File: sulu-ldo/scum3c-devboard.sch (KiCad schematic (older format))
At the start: 36 parts, among them J1 Conn_02x11_Odd_Even, J2 Conn_02x10_Odd_Even, J3 Conn_02x05_Odd_Even, J4 Conn_01x01_Male, U2 S-85S1AB18-I6T1U, U3 S-85S1AB11-I6T1U, U9AB1 ICM-20948

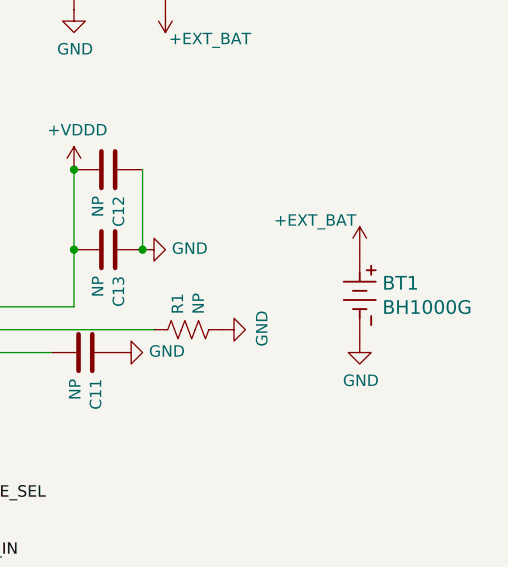
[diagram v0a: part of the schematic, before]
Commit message: updated ldo with 3d model from reg
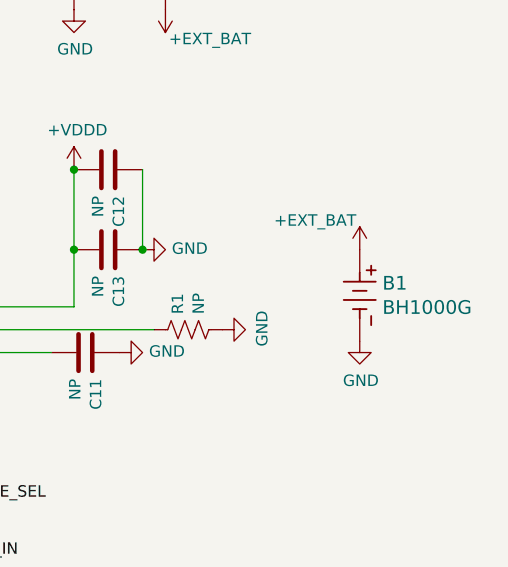
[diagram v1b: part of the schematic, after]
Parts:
- removed BT1: BH1000G, downloaded_libs:BH1000G, symbol BH1000G:BH1000G
- added B1: BH1000G, downloaded_libs:BH1000G, symbol BH1000G:BH1000G
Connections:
- net +EXT_BAT: now also B1.2
- net GND: now also B1.1
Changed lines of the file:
@@
-$EndComp
-$Comp
-L BH1000G:BH1000G BT1
-U 1 1 61316963
-P 10000 2400
-F 0 "BT1" V 10147 2499 60  0000 L CNN
-F 1 "BH1000G" V 10253 2499 60  0000 L CNN
-F 2 "downloaded_libs:BH1000G" H 10150 2040 60  0001 C CNN
-F 3 "" H 10000 2400 60  0000 C CNN
-	1    10000 2400
-	0    1    1    0
 $EndComp
 $Comp
@@
 Text Label 1200 5300 2    50   ~ 0
 1.1V_IN
+$Comp
+L BH1000G:BH1000G B1
+U 1 1 6131F561
+P 10000 2400
+F 0 "B1" V 10147 2499 60  0000 L CNN
+F 1 "BH1000G" V 10253 2499 60  0000 L CNN
+F 2 "downloaded_libs:BH1000G" H 10150 2040 60  0001 C CNN
+F 3 "" H 10000 2400 60  0000 C CNN
+	1    10000 2400
+	0    1    1    0
+$EndComp
 $EndSCHEMATC

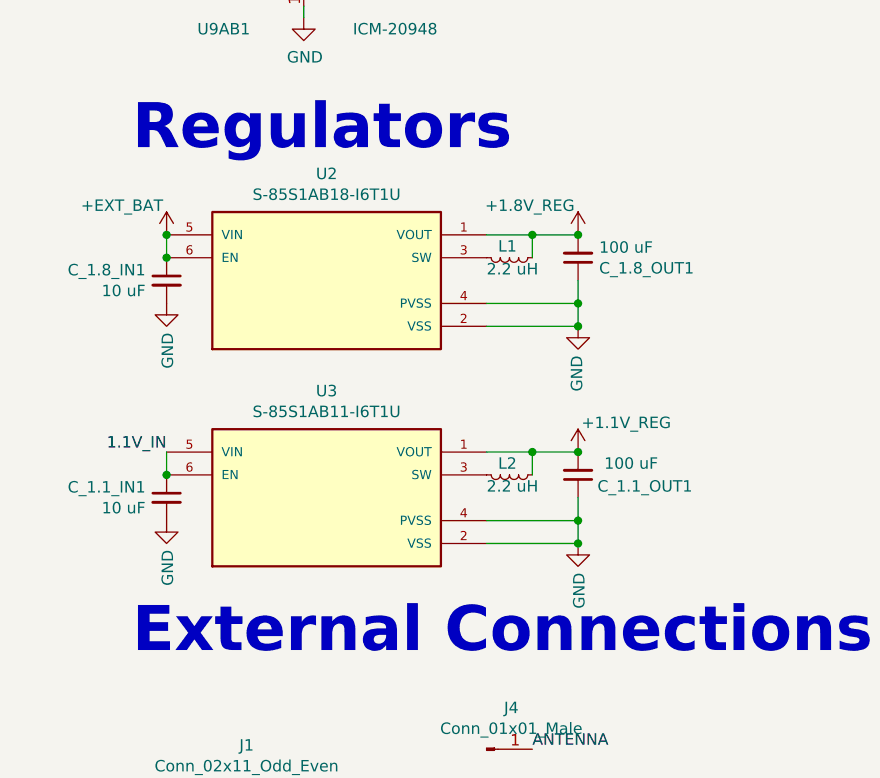
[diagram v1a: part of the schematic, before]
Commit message: checked out ldo version from ldo branch
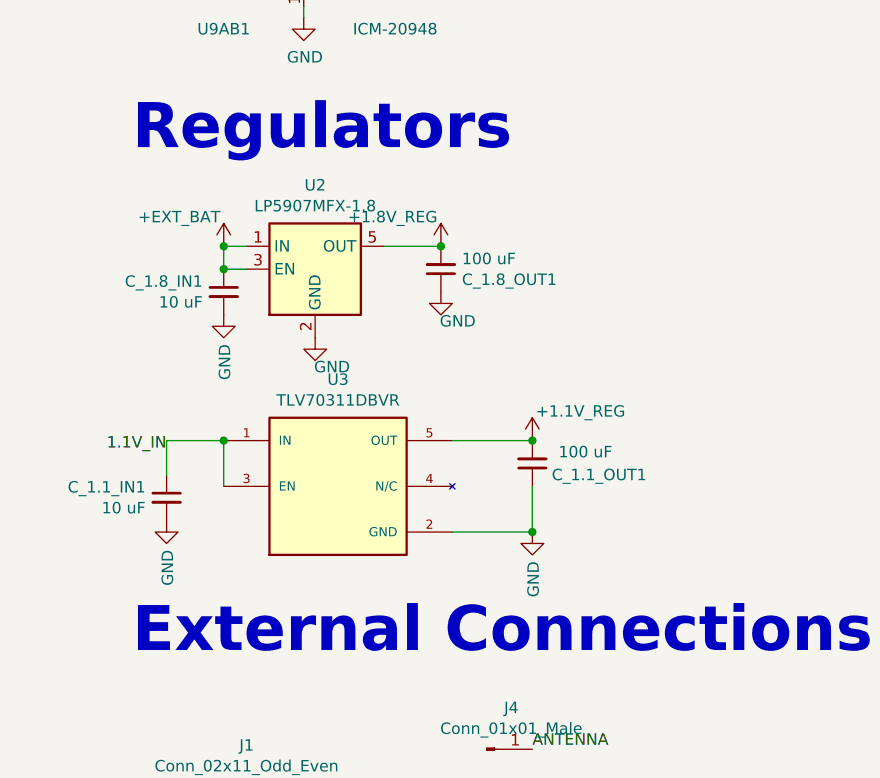
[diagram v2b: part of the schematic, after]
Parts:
- removed L1, L2: 2.2 uH, Inductor_SMD:L_0402_1005Metric, symbol Device:L_Small
- removed U2: S-85S1AB18-I6T1U, downloaded_libs:SOFL50P180X50-6N, symbol S-85S1AB20-I6T1U:S-85S1AB18-I6T1U
- removed U3: S-85S1AB11-I6T1U, downloaded_libs:SOFL50P180X50-6N, symbol S-85S1AB20-I6T1U:S-85S1AB11-I6T1U
- added U2: LP5907MFX-1.8, Package_TO_SOT_SMD:SOT-23-5, symbol Regulator_Linear:LP5907MFX-1.8
- added U3: TLV70311DBVR, downloaded_libs:SOT95P280X145-5N, symbol TLV70311DBVR:TLV70311DBVR
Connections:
- net +1.1V_REG: now also U3.5 (OUT)
- net +1.8V_REG: now also U2.5 (OUT)
- net +EXT_BAT: now also U2.1 (IN), U2.3 (EN)
- net 1.1V_IN: now also U3.1 (IN), U3.3 (EN)
- net GND: now also U2.2 (GND), U3.2 (GND)
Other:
- moved on the sheet: C_1.1_OUT1, C_1.8_IN1, C_1.8_OUT1
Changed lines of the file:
@@
 L power:GND #PWR?
 U 1 1 61293282
-P 3000 4750
+P 1850 4800
 AR Path="/5F3B307E/61293282" Ref="#PWR?"  Part="1"
 AR Path="/61293282" Ref="#PWR0115"  Part="1"
-F 0 "#PWR0115" H 3000 4500 50  0001 C CNN
-F 1 "GND" V 3005 4622 50  0000 R CNN
-F 2 "" H 3000 4750 50  0001 C CNN
-F 3 "" H 3000 4750 50  0001 C CNN
-	1    3000 4750
+F 0 "#PWR0115" H 1850 4550 50  0001 C CNN
+F 1 "GND" H 1855 4672 50  0000 R CNN
+F 2 "" H 1850 4800 50  0001 C CNN
+F 3 "" H 1850 4800 50  0001 C CNN
+	1    1850 4800
 	-1   0    0    -1
 $EndComp
@@
 L Device:C_Small C_1.8_OUT1
 U 1 1 612968B6
-P 3000 4450
-F 0 "C_1.8_OUT1" H 3092 4496 50  0000 L CNN
-F 1 "100 uF" H 3092 4405 50  0000 L CNN
-F 2 "Capacitor_SMD:C_0805_2012Metric" H 3000 4450 50  0001 C CNN
-F 3 "~" H 3000 4450 50  0001 C CNN
-	1    3000 4450
+P 2400 4500
+F 0 "C_1.8_OUT1" H 2492 4546 50  0000 L CNN
+F 1 "100 uF" H 2492 4455 50  0000 L CNN
+F 2 "Capacitor_SMD:C_0805_2012Metric" H 2400 4500 50  0001 C CNN
+F 3 "~" H 2400 4500 50  0001 C CNN
+	1    2400 4500
 	1    0    0    1
-$EndComp
-$Comp
-L Device:L_Small L1
-U 1 1 6129713D
-P 2700 4450
-F 0 "L1" V 2650 4400 50  0000 L CNN
-F 1 "2.2 uH" V 2750 4350 50  0000 L CNN
-F 2 "Inductor_SMD:L_0402_1005Metric" H 2700 4450 50  0001 C CNN
-F 3 "~" H 2700 4450 50  0001 C CNN
-	1    2700 4450
-	0    1    1    0
 $EndComp
 $Comp
@@
 L Device:C_Small C_1.1_OUT1
 U 1 1 612ACBE1
-P 3000 5400
-F 0 "C_1.1_OUT1" H 3500 5450 50  0000 R CNN
-F 1 "100 uF" H 3350 5350 50  0000 R CNN
-F 2 "Capacitor_SMD:C_0805_2012Metric" H 3000 5400 50  0001 C CNN
-F 3 "~" H 3000 5400 50  0001 C CNN
-	1    3000 5400
+P 2800 5350
+F 0 "C_1.1_OUT1" H 3300 5400 50  0000 R CNN
+F 1 "100 uF" H 3150 5300 50  0000 R CNN
+F 2 "Capacitor_SMD:C_0805_2012Metric" H 2800 5350 50  0001 C CNN
+F 3 "~" H 2800 5350 50  0001 C CNN
+	1    2800 5350
 	1    0    0    1
-$EndComp
-$Comp
-L Device:L_Small L2
-U 1 1 612ACBE7
-P 2700 5400
-F 0 "L2" V 2650 5350 50  0000 L CNN
-F 1 "2.2 uH" V 2750 5300 50  0000 L CNN
-F 2 "Inductor_SMD:L_0402_1005Metric" H 2700 5400 50  0001 C CNN
-F 3 "~" H 2700 5400 50  0001 C CNN
-	1    2700 5400
-	0    1    1    0
 $EndComp
 $Comp
@@
 L power:GND #PWR?
 U 1 1 612ACC04
-P 3000 5700
+P 2800 5650
 AR Path="/5F3B307E/612ACC04" Ref="#PWR?"  Part="1"
 AR Path="/612ACC04" Ref="#PWR0120"  Part="1"
-F 0 "#PWR0120" H 3000 5450 50  0001 C CNN
-F 1 "GND" V 3005 5572 50  0000 R CNN
-F 2 "" H 3000 5700 50  0001 C CNN
-F 3 "" H 3000 5700 50  0001 C CNN
-	1    3000 5700
+F 0 "#PWR0120" H 2800 5400 50  0001 C CNN
+F 1 "GND" V 2805 5522 50  0000 R CNN
+F 2 "" H 2800 5650 50  0001 C CNN
+F 3 "" H 2800 5650 50  0001 C CNN
+	1    2800 5650
 	1    0    0    -1
 $EndComp
@@
 L draft1library:+1.1V_REG #PWR0121
 U 1 1 612B51DE
-P 3000 5300
-F 0 "#PWR0121" H 3000 5150 50  0001 C CNN
-F 1 "+1.1V_REG" H 3015 5428 50  0000 L CNN
-F 2 "" H 3000 5300 50  0001 C CNN
-F 3 "" H 3000 5300 50  0001 C CNN
-	1    3000 5300
+P 2800 5250
+F 0 "#PWR0121" H 2800 5100 50  0001 C CNN
+F 1 "+1.1V_REG" H 2815 5378 50  0000 L CNN
+F 2 "" H 2800 5250 50  0001 C CNN
+F 3 "" H 2800 5250 50  0001 C CNN
+	1    2800 5250
 	1    0    0    -1
 $EndComp
@@
 L draft1library:+1.8V_REG #PWR0122
 U 1 1 612B5F52
-P 3000 4350
-F 0 "#PWR0122" H 3000 4200 50  0001 C CNN
-F 1 "+1.8V_REG" H 3015 4478 50  0000 L CNN
-F 2 "" H 3000 4350 50  0001 C CNN
-F 3 "" H 3000 4350 50  0001 C CNN
-	1    3000 4350
-	-1   0    0    -1
-$EndComp
-Connection ~ 3000 4350
-Wire Wire Line
-	1200 4350 1200 4450
-Connection ~ 1200 4450
+P 2400 4400
+F 0 "#PWR0122" H 2400 4250 50  0001 C CNN
+F 1 "+1.8V_REG" H 2415 4528 50  0000 L CNN
+F 2 "" H 2400 4400 50  0001 C CNN
+F 3 "" H 2400 4400 50  0001 C CNN
+	1    2400 4400
+	-1   0    0    -1
+$EndComp
+Wire Wire Line
+	1450 4400 1450 4500
 $Comp
 L draft1library:+EXT_BAT #PWR0124
 U 1 1 612B9C56
-P 1200 4350
-F 0 "#PWR0124" H 1200 4200 50  0001 C CNN
-F 1 "+EXT_BAT" H 1215 4478 50  0000 L CNN
-F 2 "" H 1200 4350 50  0001 C CNN
-F 3 "" H 1200 4350 50  0001 C CNN
-	1    1200 4350
-	-1   0    0    -1
-$EndComp
-Connection ~ 1200 4350
+P 1450 4400
+F 0 "#PWR0124" H 1450 4250 50  0001 C CNN
+F 1 "+EXT_BAT" H 1465 4528 50  0000 L CNN
+F 2 "" H 1450 4400 50  0001 C CNN
+F 3 "" H 1450 4400 50  0001 C CNN
+	1    1450 4400
+	-1   0    0    -1
+$EndComp
 Text Notes 1050 4000 0    197  ~ 39
 Regulators
@@
 L Device:C_Small C_1.8_IN1
 U 1 1 612980CF
-P 1200 4550
-F 0 "C_1.8_IN1" H 1292 4596 50  0000 L CNN
-F 1 "10 uF" H 1292 4505 50  0000 L CNN
-F 2 "Capacitor_SMD:C_0402_1005Metric" H 1200 4550 50  0001 C CNN
-F 3 "~" H 1200 4550 50  0001 C CNN
-	1    1200 4550
-	-1   0    0    -1
-$EndComp
-$Comp
-L S-85S1AB20-I6T1U:S-85S1AB11-I6T1U U3
-U 1 1 613EE865
-P 1900 5500
-F 0 "U3" H 1900 5967 50  0000 C CNN
-F 1 "S-85S1AB11-I6T1U" H 1900 5876 50  0000 C CNN
-F 2 "downloaded_libs:SOFL50P180X50-6N" H 1900 5500 50  0001 L BNN
-F 3 "downloaded_libs/S85S1A_E.pdf" H 1900 5500 50  0001 L BNN
-F 4 "0.50 mm" H 1900 5500 50  0001 L BNN "MAXIMUM_PACKAGE_HEIGHT"
-F 5 "ABLIC U.S.A. Inc." H 1900 5500 50  0001 L BNN "MANUFACTURER"
-F 6 "1.4_00" H 1900 5500 50  0001 L BNN "PARTREV"
-F 7 "IPC 7351B" H 1900 5500 50  0001 L BNN "STANDARD"
-	1    1900 5500
-	1    0    0    -1
-$EndComp
-$Comp
-L S-85S1AB20-I6T1U:S-85S1AB18-I6T1U U2
-U 1 1 613EFF3D
-P 1900 4550
-F 0 "U2" H 1900 5017 50  0000 C CNN
-F 1 "S-85S1AB18-I6T1U" H 1900 4926 50  0000 C CNN
-F 2 "downloaded_libs:SOFL50P180X50-6N" H 1900 4550 50  0001 L BNN
-F 3 "downloaded_libs/S85S1A_E.pdf" H 1900 4550 50  0001 L BNN
-F 4 "0.50 mm" H 1900 4550 50  0001 L BNN "MAXIMUM_PACKAGE_HEIGHT"
-F 5 "ABLIC U.S.A. Inc." H 1900 4550 50  0001 L BNN "MANUFACTURER"
-F 6 "1.4_00" H 1900 4550 50  0001 L BNN "PARTREV"
-F 7 "IPC 7351B" H 1900 4550 50  0001 L BNN "STANDARD"
-	1    1900 4550
-	1    0    0    -1
+P 1450 4600
+F 0 "C_1.8_IN1" H 1542 4646 50  0000 L CNN
+F 1 "10 uF" H 1542 4555 50  0000 L CNN
+F 2 "Capacitor_SMD:C_0402_1005Metric" H 1450 4600 50  0001 C CNN
+F 3 "~" H 1450 4600 50  0001 C CNN
+	1    1450 4600
+	-1   0    0    -1
 $EndComp
 $Comp
 L power:GND #PWR?
 U 1 1 613F95E1
-P 1200 4650
+P 1450 4700
 AR Path="/5F3B307E/613F95E1" Ref="#PWR?"  Part="1"
 AR Path="/613F95E1" Ref="#PWR0117"  Part="1"
-F 0 "#PWR0117" H 1200 4400 50  0001 C CNN
-F 1 "GND" V 1205 4522 50  0000 R CNN
-F 2 "" H 1200 4650 50  0001 C CNN
-F 3 "" H 1200 4650 50  0001 C CNN
-	1    1200 4650
-	1    0    0    -1
-$EndComp
-Wire Wire Line
-	3000 4350 2800 4350
-Wire Wire Line
-	2600 4750 3000 4750
-Wire Wire Line
-	3000 4650 3000 4550
-Wire Wire Line
-	2600 4650 3000 4650
-Wire Wire Line
-	3000 4750 3000 4650
-Connection ~ 3000 4750
-Connection ~ 3000 4650
-Wire Wire Line
-	2600 5300 2800 5300
-Wire Wire Line
-	1200 5300 1200 5400
-Connection ~ 1200 5400
-Connection ~ 3000 5300
-Wire Wire Line
-	2600 5600 3000 5600
-Wire Wire Line
-	3000 5600 3000 5500
-Wire Wire Line
-	3000 5600 3000 5700
-Connection ~ 3000 5600
-Wire Wire Line
-	2600 5700 3000 5700
-Connection ~ 3000 5700
+F 0 "#PWR0117" H 1450 4450 50  0001 C CNN
+F 1 "GND" V 1455 4572 50  0000 R CNN
+F 2 "" H 1450 4700 50  0001 C CNN
+F 3 "" H 1450 4700 50  0001 C CNN
+	1    1450 4700
+	1    0    0    -1
+$EndComp
 $Comp
 L power:GND #PWR046
@@
 	1    0    0    -1
 $EndComp
-Wire Wire Line
-	2800 5400 2800 5300
-Connection ~ 2800 5300
-Wire Wire Line
-	2800 5300 3000 5300
-Wire Wire Line
-	2800 4450 2800 4350
-Connection ~ 2800 4350
-Wire Wire Line
-	2800 4350 2600 4350
 $Comp
 L draft1library:+EXT_BAT #PWR0116
@@
 	0    1    1    0
 $EndComp
+$Comp
+L Regulator_Linear:LP5907MFX-1.8 U2
+U 1 1 6131C2EC
+P 1850 4500
+F 0 "U2" H 1850 4867 50  0000 C CNN
+F 1 "LP5907MFX-1.8" H 1850 4776 50  0000 C CNN
+F 2 "Package_TO_SOT_SMD:SOT-23-5" H 1850 4850 50  0001 C CNN
+F 3 "http://www.ti.com/lit/ds/symlink/lp5907.pdf" H 1850 5000 50  0001 C CNN
+	1    1850 4500
+	1    0    0    -1
+$EndComp
+Wire Wire Line
+	1550 4400 1450 4400
+Connection ~ 1450 4400
+Wire Wire Line
+	1550 4500 1450 4500
+Connection ~ 1450 4500
+$Comp
+L power:GND #PWR?
+U 1 1 61327393
+P 2400 4600
+AR Path="/5F3B307E/61327393" Ref="#PWR?"  Part="1"
+AR Path="/61327393" Ref="#PWR0129"  Part="1"
+F 0 "#PWR0129" H 2400 4350 50  0001 C CNN
+F 1 "GND" H 2405 4472 50  0000 R CNN
+F 2 "" H 2400 4600 50  0001 C CNN
+F 3 "" H 2400 4600 50  0001 C CNN
+	1    2400 4600
+	-1   0    0    -1
+$EndComp
+Wire Wire Line
+	2150 4400 2400 4400
+Connection ~ 2400 4400
+$Comp
+L TLV70311DBVR:TLV70311DBVR U3
+U 1 1 6132BD9C
+P 1950 5450
+F 0 "U3" H 1950 5917 50  0000 C CNN
+F 1 "TLV70311DBVR" H 1950 5826 50  0000 C CNN
+F 2 "downloaded_libs:SOT95P280X145-5N" H 1950 5450 50  0001 L BNN
+F 3 "" H 1950 5450 50  0001 L BNN
+F 4 "1.45mm" H 1950 5450 50  0001 L BNN "MAXIMUM_PACKAGE_HEIGHT"
+F 5 "IPC-7351B" H 1950 5450 50  0001 L BNN "STANDARD"
+F 6 "O" H 1950 5450 50  0001 L BNN "PARTREV"
+F 7 "Texas Instruments" H 1950 5450 50  0001 L BNN "MANUFACTURER"
+	1    1950 5450
+	1    0    0    -1
+$EndComp
+Wire Wire Line
+	1450 5250 1450 5450
+Wire Wire Line
+	1200 5250 1450 5250
+Wire Wire Line
+	1200 5250 1200 5400
+Connection ~ 1450 5250
+Wire Wire Line
+	2800 5450 2800 5650
+Wire Wire Line
+	2450 5650 2800 5650
+Connection ~ 2800 5650
+Wire Wire Line
+	2450 5250 2800 5250
+Connection ~ 2800 5250
 $EndSCHEMATC
